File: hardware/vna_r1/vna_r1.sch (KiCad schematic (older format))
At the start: 0 parts

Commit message: layout on vna r1 control board
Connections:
- net labels added: 3V3_DEMOD_EXT_EN
- net labels removed: 3V3_RF_SENSE, AMP_5V, PANEL_PORT1_LED, PANEL_PORT2_LED, PORT1_BIAS, PORT2_BIAS, SPI_CLK, SPI_SDI
- wire segments 193 -> 153
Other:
- note added: "microwave vector network analyzer control board"
- note removed: "microwave vector network analyzer"

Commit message: added adrf5020 breakout
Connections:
- net labels removed: PANEL_POWER_LED
- wire segments 153 -> 151
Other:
- note added: "use Molex Picoblade?\n0151341400\n"
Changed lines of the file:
@@
 F0 "power" 60
 F1 "power.sch" 60
-F4 "3V3_DEMOD_SENSE" I R 3550 2400 60
-F6 "3V3_DEMOD_EN" I L 1650 1800 60
-F9 "3V3_PLL_EN" I L 1650 1900 60
-F10 "3V3_PLL_SENSE" I R 3550 2600 60
+F2 "3V3_DEMOD_SENSE" I R 3550 2400 60
+F3 "3V3_DEMOD_EN" I L 1650 1800 60
+F4 "3V3_PLL_EN" I L 1650 1900 60
+F5 "3V3_PLL_SENSE" I R 3550 2600 60
 $EndSheet
 $Sheet
@@
 F4 "DEMOD_3" O L 12500 7600 60
 F5 "DEMOD_4" O L 12500 9700 60
-F6 "POWER_LED" I R 13800 9400 60
 $EndSheet
 Text Label 14150 6600 0    60   ~ 0
@@
 Text Label 14600 5700 0    60   ~ 0
 RF_SPI_SDI
-Text Label 14000 9400 0    60   ~ 0
-PANEL_POWER_LED
 Text Label 14300 4300 0    60   ~ 0
 PORT_SEL
@@
 Text Label 1500 7350 2    60   ~ 0
 AD_CLKOUT
-Text Label 1500 8900 2    60   ~ 0
-PANEL_POWER_LED
 Text Label 4800 8850 2    60   ~ 0
 EXT_PLL_REF
@@
 F30 "AD_PD" O L 1650 6900 60
 F31 "AD_PC" O L 1650 7000 60
-F32 "PANEL_POWER_LED" O L 1650 8900 60
 F33 "EXT_IO_0" B R 3550 10300 60
 F34 "EXT_IO_1" B R 3550 10400 60
@@
 	9250 10700 9450 10700
 Wire Wire Line
-	13800 9400 14000 9400
-Wire Wire Line
 	4800 8600 5000 8600
 Wire Wire Line
@@
 Wire Wire Line
 	1500 8500 1650 8500
-Wire Wire Line
-	1500 8900 1650 8900
 Wire Wire Line
 	1500 6450 1650 6450
@@
 Text Label 14300 8700 0    60   ~ 0
 3V3_DEMOD_EXT_EN
+Text Notes 14600 7050 0    60   ~ 0
+use Molex Picoblade?\n0151341400\n
 $EndSCHEMATC

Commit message: more work on vna r1..
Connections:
- net labels added: 3V3_LO_EN, LO_-5V_EN, LO_AMP_EN, LO_DAC_CS, LO_PORT_SEL, RF_-5V_EN, RF_PORT_SEL
- net labels removed: -5V_EN, PORT_SEL
- wire segments 151 -> 153
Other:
- note removed: "use Molex Picoblade?\n0151341400\n"
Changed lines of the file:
@@
 F5 "3V3_PLL_SENSE" I R 3550 2600 60
 $EndSheet
-$Sheet
-S 12500 950  1300 8900
-U 59CEBE41
-F0 "front_panel" 60
-F1 "front_panel.sch" 60
-F2 "DEMOD_1" O L 12500 3450 60
-F3 "DEMOD_2" O L 12500 5550 60
-F4 "DEMOD_3" O L 12500 7600 60
-F5 "DEMOD_4" O L 12500 9700 60
-$EndSheet
-Text Label 14150 6600 0    60   ~ 0
+Text Label 14400 8350 0    60   ~ 0
 SYNTH_REF_AP
-Text Label 14150 6700 0    60   ~ 0
+Text Label 14400 8450 0    60   ~ 0
 SYNTH_REF_AN
-Text Label 14550 7950 0    60   ~ 0
+Text Label 14400 8700 0    60   ~ 0
 SYNTH_REF_BP
-Text Label 14550 8050 0    60   ~ 0
+Text Label 14400 8800 0    60   ~ 0
 SYNTH_REF_BN
 Text Label 9250 3400 2    60   ~ 0
@@
 Text Label 9250 9500 2    60   ~ 0
 IF_REF_D
-Text Label 14300 8500 0    60   ~ 0
+Text Label 14350 9050 0    60   ~ 0
 MIX_X2
-Text Label 14300 8600 0    60   ~ 0
+Text Label 14350 9150 0    60   ~ 0
 MIX_EN
 Text Label 9250 5850 2    60   ~ 0
@@
 NoConn ~ 9250 10500
 NoConn ~ 9250 10700
-Text Label 14550 7750 0    60   ~ 0
+Text Label 14350 7600 0    60   ~ 0
 LO_SYNTH_LOCK
-Text Label 14550 7350 0    60   ~ 0
+Text Label 14350 7300 0    60   ~ 0
 LO_SYNTH_CE
-Text Label 14550 7450 0    60   ~ 0
+Text Label 14350 7400 0    60   ~ 0
 LO_SYNTH_CS
-Text Label 14550 7550 0    60   ~ 0
+Text Label 14350 7800 0    60   ~ 0
 LO_SPI_CLK
-Text Label 14550 7650 0    60   ~ 0
+Text Label 14350 7500 0    60   ~ 0
 LO_SPI_SDI
-Text Label 14600 5400 0    60   ~ 0
+Text Label 14350 6400 0    60   ~ 0
 RF_SYNTH_LOCK
-Text Label 14600 5200 0    60   ~ 0
+Text Label 14350 6100 0    60   ~ 0
 RF_SYNTH_CE
-Text Label 14600 5300 0    60   ~ 0
+Text Label 14350 6200 0    60   ~ 0
 RF_SYNTH_CS
-Text Label 14600 5600 0    60   ~ 0
+Text Label 14350 6550 0    60   ~ 0
 RF_SPI_CLK
-Text Label 14600 5500 0    60   ~ 0
+Text Label 14350 6500 0    60   ~ 0
 RF_DAC_CS
-Text Label 14600 5700 0    60   ~ 0
+Text Label 14350 6300 0    60   ~ 0
 RF_SPI_SDI
-Text Label 14300 4300 0    60   ~ 0
-PORT_SEL
+Text Label 14350 5600 0    60   ~ 0
+RF_PORT_SEL
 Text Label 1500 3200 2    60   ~ 0
-PORT_SEL
+RF_PORT_SEL
 Text Label 7100 9700 0    60   ~ 0
 ADC_CLK_D
@@
 Text Label 1500 5400 2    60   ~ 0
 SCL
-Text Label 14600 5950 0    60   ~ 0
+Text Label 14350 5900 0    60   ~ 0
 RF_FILT_SW_1
-Text Label 14650 6250 0    60   ~ 0
+Text Label 14350 7100 0    60   ~ 0
 RF_FILT_SW_2
 Text Label 3750 2400 0    60   ~ 0
@@
 Text Label 3750 2600 0    60   ~ 0
 3V3_PLL_SENSE
-Text Label 14300 4400 0    60   ~ 0
--5V_EN
-Text Label 14300 4500 0    60   ~ 0
+Text Label 14350 5700 0    60   ~ 0
+RF_-5V_EN
+Text Label 14350 5800 0    60   ~ 0
 RF_AMP_EN
-Text Label 14600 5000 0    60   ~ 0
+Text Label 14350 6000 0    60   ~ 0
 3V3_RF_EN
 Text Label 1450 1800 2    60   ~ 0
@@
 RF_FILT_SW_2
 Text Label 1500 5550 2    60   ~ 0
--5V_EN
+RF_-5V_EN
 Text Label 1500 5650 2    60   ~ 0
 RF_AMP_EN
@@
 F30 "AD_PD" O L 1650 6900 60
 F31 "AD_PC" O L 1650 7000 60
-F33 "EXT_IO_0" B R 3550 10300 60
-F34 "EXT_IO_1" B R 3550 10400 60
-F35 "EXT_IO_2" B R 3550 10500 60
-F36 "EXT_IO_3" B R 3550 10600 60
-F37 "EXT_SPI_CS1" O R 3550 9350 60
-F38 "EXT_SPI_CS0" O R 3550 9250 60
-F39 "EXT_SPI_CLK" O R 3550 9600 60
-F40 "EXT_SPI_MISO" I R 3550 9500 60
-F41 "EXT_SPI_MOSI" O R 3550 9700 60
-F42 "EXT_AIN0" I R 3550 10750 60
-F43 "EXT_AIN1" I R 3550 10850 60
-F44 "RF_DAC_CS" O L 1650 4500 60
-F45 "LO_SYNTH_LOCK" O L 1650 4850 60
-F46 "LO_SYNTH_CE" O L 1650 4650 60
-F47 "LO_SYNTH_CS" O L 1650 4750 60
-F48 "EXT_UART_MTX" O R 3550 9950 60
-F49 "EXT_UART_MRX" I R 3550 9850 60
-F50 "LO_SPI_CLK" O L 1650 5000 60
-F51 "LO_SPI_SDI" O L 1650 5100 60
-F52 "RF_SPI_CLK" O L 1650 3600 60
-F53 "RF_SPI_SDI" O L 1650 3700 60
-F54 "EXT_TRIG" I R 3550 10100 60
-F55 "3V3_EXT_DEMOD_EN" O L 1650 6050 61
+F32 "EXT_IO_0" B R 3550 10300 60
+F33 "EXT_IO_1" B R 3550 10400 60
+F34 "EXT_IO_2" B R 3550 10500 60
+F35 "EXT_IO_3" B R 3550 10600 60
+F36 "EXT_SPI_CS1" O R 3550 9350 60
+F37 "EXT_SPI_CS0" O R 3550 9250 60
+F38 "EXT_SPI_CLK" O R 3550 9600 60
+F39 "EXT_SPI_MISO" I R 3550 9500 60
+F40 "EXT_SPI_MOSI" O R 3550 9700 60
+F41 "EXT_AIN0" I R 3550 10750 60
+F42 "EXT_AIN1" I R 3550 10850 60
+F43 "RF_DAC_CS" O L 1650 4500 60
+F44 "LO_SYNTH_LOCK" O L 1650 4850 60
+F45 "LO_SYNTH_CE" O L 1650 4650 60
+F46 "LO_SYNTH_CS" O L 1650 4750 60
+F47 "EXT_UART_MTX" O R 3550 9950 60
+F48 "EXT_UART_MRX" I R 3550 9850 60
+F49 "LO_SPI_CLK" O L 1650 5000 60
+F50 "LO_SPI_SDI" O L 1650 5100 60
+F51 "RF_SPI_CLK" O L 1650 3600 60
+F52 "RF_SPI_SDI" O L 1650 3700 60
+F53 "EXT_TRIG" I R 3550 10100 60
+F54 "3V3_EXT_DEMOD_EN" O L 1650 6050 61
 $EndSheet
 Text Label 14800 1950 2    60   ~ 0
@@
 	11150 3450 12500 3450
 Wire Wire Line
-	14150 6600 13950 6600
-Wire Wire Line
-	14150 6700 13950 6700
-Wire Wire Line
-	14550 7950 14350 7950
-Wire Wire Line
-	14550 8050 14350 8050
-Wire Wire Line
-	14550 7650 14350 7650
-Wire Wire Line
-	14550 7750 14350 7750
-Wire Wire Line
-	14550 7450 14350 7450
-Wire Wire Line
-	14550 7550 14350 7550
-Wire Wire Line
-	14550 7350 14350 7350
-Wire Wire Line
-	14600 5400 14400 5400
-Wire Wire Line
-	14600 5300 14400 5300
-Wire Wire Line
-	14600 5200 14400 5200
-Wire Wire Line
-	14600 5950 14400 5950
-Wire Wire Line
-	14650 6250 14450 6250
-Wire Wire Line
-	14600 5600 14400 5600
-Wire Wire Line
-	14600 5700 14400 5700
-Wire Wire Line
-	14600 5500 14400 5500
+	14400 8350 14200 8350
+Wire Wire Line
+	14400 8450 14200 8450
+Wire Wire Line
+	14400 8700 14200 8700
+Wire Wire Line
+	14400 8800 14200 8800
+Wire Wire Line
+	14350 7500 14150 7500
+Wire Wire Line
+	14350 7600 14150 7600
+Wire Wire Line
+	14350 7400 14150 7400
+Wire Wire Line
+	14350 7800 14150 7800
+Wire Wire Line
+	14350 7300 14150 7300
+Wire Wire Line
+	14350 6400 14150 6400
+Wire Wire Line
+	14350 6200 14150 6200
+Wire Wire Line
+	14350 6100 14150 6100
+Wire Wire Line
+	14350 5900 14150 5900
+Wire Wire Line
+	14350 7100 14150 7100
+Wire Wire Line
+	14350 6550 14150 6550
+Wire Wire Line
+	14350 6300 14150 6300
+Wire Wire Line
+	14350 6500 14150 6500
 Wire Wire Line
 	9250 3250 9450 3250
@@
 	9250 9650 9450 9650
 Wire Wire Line
-	14300 8500 14100 8500
+	14350 9050 14150 9050
 Wire Wire Line
 	9250 5850 9450 5850
@@
 Wire Wire Line
 	1500 6050 1650 6050
-Text Label 14300 8700 0    60   ~ 0
+Text Label 14350 9250 0    60   ~ 0
 3V3_DEMOD_EXT_EN
-Text Notes 14600 7050 0    60   ~ 0
-use Molex Picoblade?\n0151341400\n
+Text Label 14350 7200 0    60   ~ 0
+3V3_LO_EN
+Text Label 4400 5200 2    60   ~ 0
+3V3_LO_EN
+Wire Wire Line
+	14350 7200 14150 7200
+Text Label 14350 7700 0    60   ~ 0
+LO_DAC_CS
+Wire Wire Line
+	14350 7700 14150 7700
+Text Label 4300 5400 2    60   ~ 0
+LO_DAC_CS
+Text Label 14350 6800 0    60   ~ 0
+LO_PORT_SEL
+Text Label 14350 6900 0    60   ~ 0
+LO_-5V_EN
+Text Label 14350 7000 0    60   ~ 0
+LO_AMP_EN
+Text Label 3900 5750 0    60   ~ 0
+LO_PORT_SEL
+Text Label 3900 5850 0    60   ~ 0
+LO_-5V_EN
+Text Label 3900 5950 0    60   ~ 0
+LO_AMP_EN
+$Sheet
+S 12500 950  1650 8900
+U 59CEBE41
+F0 "front_panel" 60
+F1 "front_panel.sch" 60
+F2 "DEMOD_1" O L 12500 3450 60
+F3 "DEMOD_2" O L 12500 5550 60
+F4 "DEMOD_3" O L 12500 7600 60
+F5 "DEMOD_4" O L 12500 9700 60
+F6 "RF_PORT_SEL" I R 14150 5550 60
+F7 "RF_-5V_EN" I R 14150 5650 60
+F8 "RF_AMP_EN" I R 14150 5750 60
+F9 "RF_FILT_SW_1" I R 14150 5850 60
+F10 "RF_3V3_EN" I R 14150 5950 60
+F11 "RF_SYNTH_CE" I R 14150 6050 60
+F12 "RF_SYNTH_CS" I R 14150 6150 60
+F13 "RF_SYNTH_SDI" I R 14150 6250 60
+F14 "RF_SYNTH_LOCK" I R 14150 6350 60
+F15 "RF_DAC_CS" I R 14150 6450 60
+F16 "LO_PORT_SEL" I R 14150 6800 60
+F17 "LO_-5V_EN" I R 14150 6900 60
+F18 "LO_AMP_EN" I R 14150 7000 60
+F19 "LO_FILT_SW_1" I R 14150 7100 60
+F20 "LO_3V3_EN" I R 14150 7200 60
+F21 "LO_SYNTH_CE" I R 14150 7300 60
+F22 "LO_SYNTH_CS" I R 14150 7400 60
+F23 "LO_SYNTH_SDI" I R 14150 7500 60
+F24 "LO_SYNTH_LOCK" I R 14150 7600 60
+F25 "LO_DAC_CS" I R 14150 7700 60
+F26 "LO_SYNTH_REF_P" I R 14150 8350 60
+F27 "LO_SYNTH_REF_N" I R 14150 8450 60
+F28 "RF_SYNTH_REF_P" I R 14150 8700 60
+F29 "RF_SYNTH_REF_N" I R 14150 8800 60
+F30 "MIX_X2" I R 14150 9050 60
+F31 "MIX_EN" I R 14150 9150 60
+F32 "MIX_3V3_EN" I R 14150 9250 60
+F33 "LO_SYNTH_CLK" I R 14150 7800 60
+F34 "RF_SYNTH_CLK" I R 14150 6550 60
+$EndSheet
 $EndSCHEMATC

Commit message: work on vna r1 synth board
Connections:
- net labels added: LO_3V3_EN, RF_3V3_EN
- net labels removed: 3V3_LO_EN, 3V3_RF_EN
- wire segments 153 -> 167

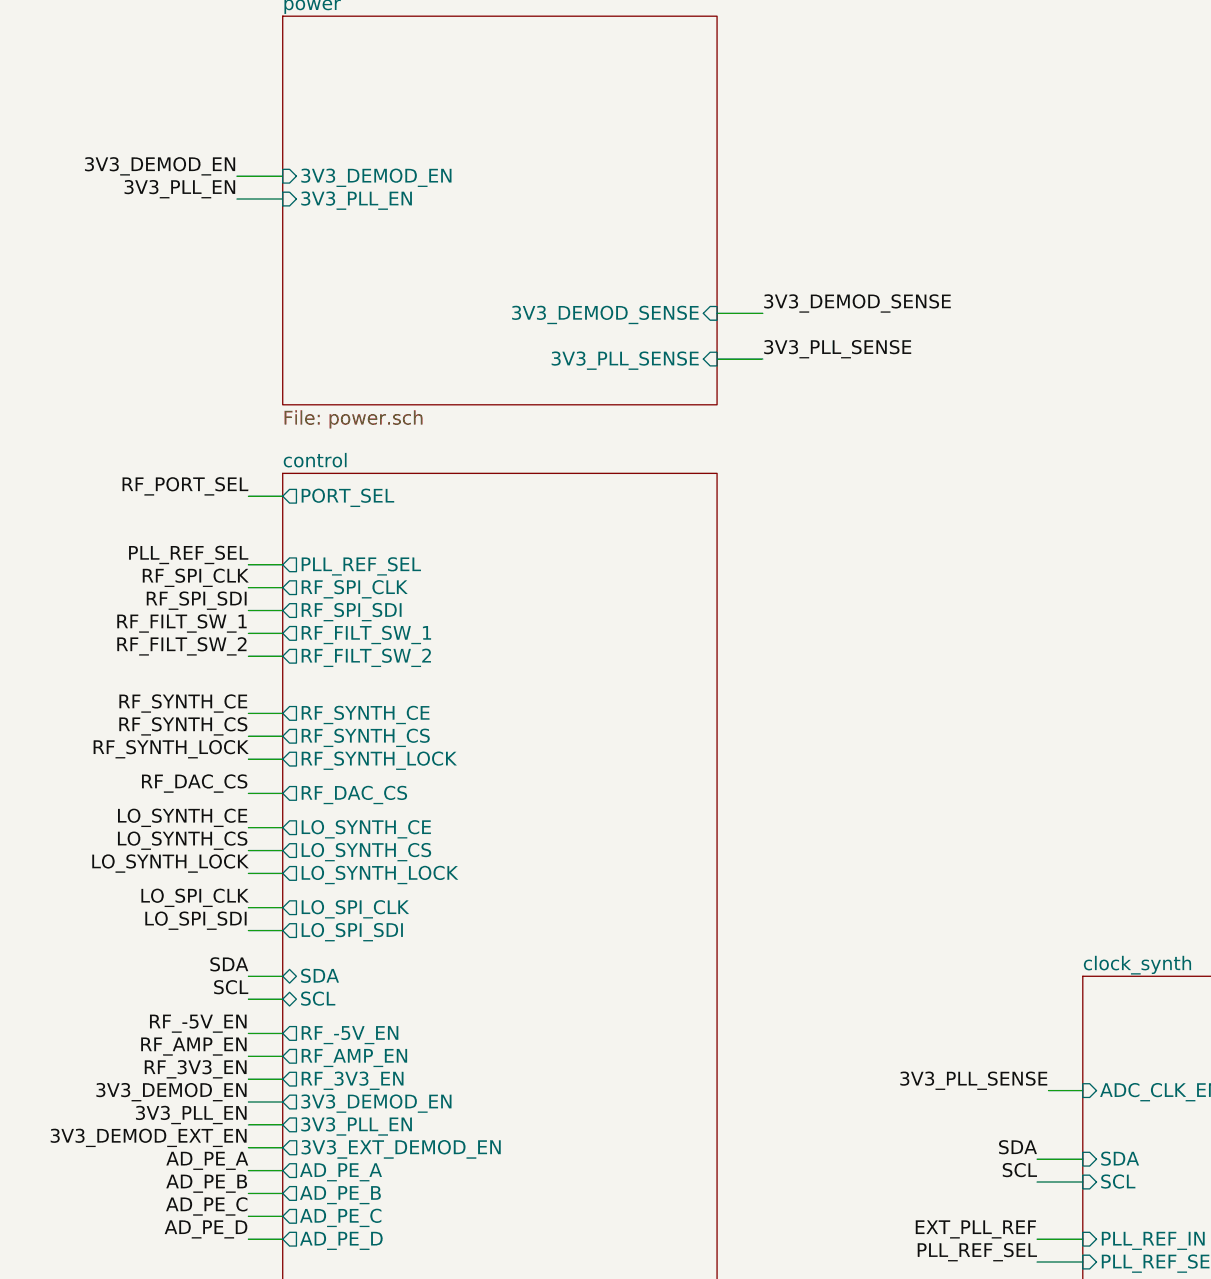
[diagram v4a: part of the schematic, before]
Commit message: added measured data on r2 directional coupler
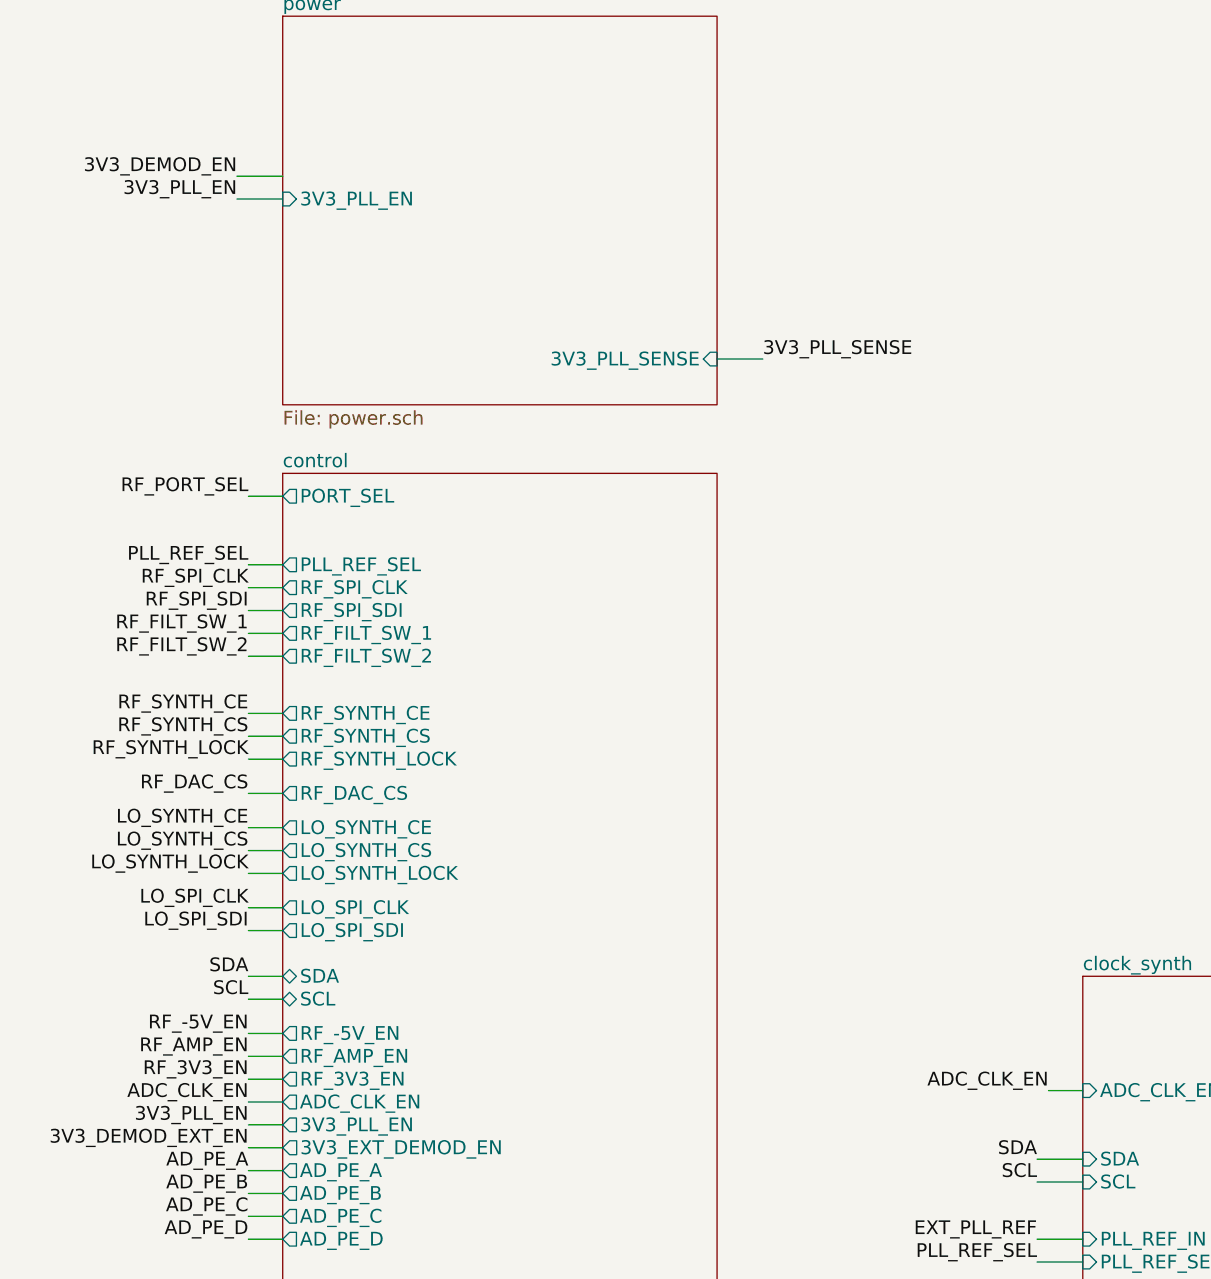
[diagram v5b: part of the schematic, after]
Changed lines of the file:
@@
 F0 "power" 60
 F1 "power.sch" 60
-F2 "3V3_DEMOD_SENSE" I R 3550 2400 60
-F3 "3V3_DEMOD_EN" I L 1650 1800 60
 F4 "3V3_PLL_EN" I L 1650 1900 60
 F5 "3V3_PLL_SENSE" I R 3550 2600 60
@@
 Text Label 14350 7100 0    60   ~ 0
 RF_FILT_SW_2
-Text Label 3750 2400 0    60   ~ 0
-3V3_DEMOD_SENSE
 Text Label 3750 2600 0    60   ~ 0
 3V3_PLL_SENSE
@@
 Text Label 1500 5750 2    60   ~ 0
 RF_3V3_EN
-Text Label 1500 5850 2    60   ~ 0
-3V3_DEMOD_EN
 Text Label 1500 5950 2    60   ~ 0
 3V3_PLL_EN
-Text Label 5000 5800 2    60   ~ 0
-3V3_PLL_SENSE
 Text Label 1500 6450 2    60   ~ 0
 AD_PE_D
@@
 F1 "control.sch" 60
 F2 "PLL_REF_SEL" O L 1650 3500 60
-F3 "3V3_DEMOD_EN" O L 1650 5850 60
-F4 "3V3_PLL_EN" O L 1650 5950 60
-F5 "RF_AMP_EN" O L 1650 5650 60
-F6 "MIX_X2" O L 1650 8400 60
-F7 "MIX_EN" O L 1650 8500 60
-F8 "AD_DOUTD" I L 1650 7850 60
-F9 "AD_DOUTC" I L 1650 7750 60
-F10 "AD_DOUTB" I L 1650 7650 60
-F11 "AD_DOUTA" I L 1650 7550 60
-F12 "AD_SYNCB" O L 1650 7150 60
-F13 "AD_FS" I L 1650 7250 60
-F14 "AD_CLKOUT" I L 1650 7350 60
-F15 "PORT_SEL" O L 1650 3200 60
-F16 "RF_FILT_SW_1" O L 1650 3800 60
-F17 "RF_FILT_SW_2" O L 1650 3900 60
-F18 "RF_SYNTH_CE" O L 1650 4150 60
-F19 "RF_SYNTH_CS" O L 1650 4250 60
-F20 "RF_SYNTH_LOCK" O L 1650 4350 60
-F21 "SCL" B L 1650 5400 60
-F22 "SDA" B L 1650 5300 60
-F23 "AD_PE_C" O L 1650 6350 60
-F24 "AD_PE_D" O L 1650 6450 60
-F25 "AD_PE_B" O L 1650 6250 60
-F26 "AD_PE_A" O L 1650 6150 60
-F27 "AD_DOUT_B" I L 1650 6800 60
-F28 "AD_PD" O L 1650 6900 60
-F29 "AD_PC" O L 1650 7000 60
-F30 "EXT_IO_0" B R 3550 10300 60
-F31 "EXT_IO_1" B R 3550 10400 60
-F32 "EXT_IO_2" B R 3550 10500 60
-F33 "EXT_IO_3" B R 3550 10600 60
-F34 "EXT_SPI_CS1" O R 3550 9350 60
-F35 "EXT_SPI_CS0" O R 3550 9250 60
-F36 "EXT_SPI_CLK" O R 3550 9600 60
-F37 "EXT_SPI_MISO" I R 3550 9500 60
-F38 "EXT_SPI_MOSI" O R 3550 9700 60
-F39 "EXT_AIN0" I R 3550 10750 60
-F40 "EXT_AIN1" I R 3550 10850 60
-F41 "RF_DAC_CS" O L 1650 4500 60
-F42 "LO_SYNTH_LOCK" O L 1650 4850 60
-F43 "LO_SYNTH_CE" O L 1650 4650 60
-F44 "LO_SYNTH_CS" O L 1650 4750 60
-F45 "EXT_UART_MTX" O R 3550 9950 60
-F46 "EXT_UART_MRX" I R 3550 9850 60
-F47 "LO_SPI_CLK" O L 1650 5000 60
-F48 "LO_SPI_SDI" O L 1650 5100 60
-F49 "RF_SPI_CLK" O L 1650 3600 60
-F50 "RF_SPI_SDI" O L 1650 3700 60
-F51 "EXT_TRIG" I R 3550 10100 60
-F52 "3V3_EXT_DEMOD_EN" O L 1650 6050 61
-F53 "RF_3V3_EN" O L 1650 5750 60
-F54 "RF_-5V_EN" O L 1650 5550 60
-F55 "LO_AMP_EN" I L 1650 8750 60
-F56 "LO_-5V_EN" I L 1650 8850 60
-F57 "LO_3V3_EN" I L 1650 8950 60
-F58 "LO_PORT_SEL" I L 1650 9050 60
-F59 "LO_DAC_CS" I L 1650 9150 60
+F3 "3V3_PLL_EN" O L 1650 5950 60
+F4 "RF_AMP_EN" O L 1650 5650 60
+F5 "MIX_X2" O L 1650 8400 60
+F6 "MIX_EN" O L 1650 8500 60
+F7 "AD_DOUTD" I L 1650 7850 60
+F8 "AD_DOUTC" I L 1650 7750 60
+F9 "AD_DOUTB" I L 1650 7650 60
+F10 "AD_DOUTA" I L 1650 7550 60
+F11 "AD_SYNCB" O L 1650 7150 60
+F12 "AD_FS" I L 1650 7250 60
+F13 "AD_CLKOUT" I L 1650 7350 60
+F14 "PORT_SEL" O L 1650 3200 60
+F15 "RF_FILT_SW_1" O L 1650 3800 60
+F16 "RF_FILT_SW_2" O L 1650 3900 60
+F17 "RF_SYNTH_CE" O L 1650 4150 60
+F18 "RF_SYNTH_CS" O L 1650 4250 60
+F19 "RF_SYNTH_LOCK" O L 1650 4350 60
+F20 "SCL" B L 1650 5400 60
+F21 "SDA" B L 1650 5300 60
+F22 "AD_PE_C" O L 1650 6350 60
+F23 "AD_PE_D" O L 1650 6450 60
+F24 "AD_PE_B" O L 1650 6250 60
+F25 "AD_PE_A" O L 1650 6150 60
+F26 "AD_DOUT_B" I L 1650 6800 60
+F27 "AD_PD" O L 1650 6900 60
+F28 "AD_PC" O L 1650 7000 60
+F29 "EXT_IO_0" B R 3550 10300 60
+F30 "EXT_IO_1" B R 3550 10400 60
+F31 "EXT_IO_2" B R 3550 10500 60
+F32 "EXT_IO_3" B R 3550 10600 60
+F33 "EXT_SPI_CS1" O R 3550 9350 60
+F34 "EXT_SPI_CS0" O R 3550 9250 60
+F35 "EXT_SPI_CLK" O R 3550 9600 60
+F36 "EXT_SPI_MISO" I R 3550 9500 60
+F37 "EXT_SPI_MOSI" O R 3550 9700 60
+F38 "EXT_AIN0" I R 3550 10750 60
+F39 "EXT_AIN1" I R 3550 10850 60
+F40 "RF_DAC_CS" O L 1650 4500 60
+F41 "LO_SYNTH_LOCK" O L 1650 4850 60
+F42 "LO_SYNTH_CE" O L 1650 4650 60
+F43 "LO_SYNTH_CS" O L 1650 4750 60
+F44 "EXT_UART_MTX" O R 3550 9950 60
+F45 "EXT_UART_MRX" I R 3550 9850 60
+F46 "LO_SPI_CLK" O L 1650 5000 60
+F47 "LO_SPI_SDI" O L 1650 5100 60
+F48 "RF_SPI_CLK" O L 1650 3600 60
+F49 "RF_SPI_SDI" O L 1650 3700 60
+F50 "EXT_TRIG" I R 3550 10100 60
+F51 "3V3_EXT_DEMOD_EN" O L 1650 6050 61
+F52 "RF_3V3_EN" O L 1650 5750 60
+F53 "RF_-5V_EN" O L 1650 5550 60
+F54 "LO_AMP_EN" I L 1650 8750 60
+F55 "LO_-5V_EN" I L 1650 8850 60
+F56 "LO_3V3_EN" I L 1650 8950 60
+F57 "LO_PORT_SEL" I L 1650 9050 60
+F58 "LO_DAC_CS" I L 1650 9150 60
+F59 "ADC_CLK_EN" O L 1650 5850 60
 $EndSheet
 Text Label 14900 1900 2    60   ~ 0
@@
 	1450 1900 1650 1900
 Wire Wire Line
-	3550 2400 3750 2400
-Wire Wire Line
 	3550 2600 3750 2600
 Wire Wire Line
@@
 Wire Wire Line
 	1500 5950 1650 5950
-Wire Wire Line
-	1500 5850 1650 5850
 Wire Wire Line
 	1500 5750 1650 5750
@@
 Wire Wire Line
 	1500 9150 1650 9150
+Text Label 5000 5800 2    60   ~ 0
+ADC_CLK_EN
+Text Label 1500 5850 2    60   ~ 0
+ADC_CLK_EN
+Wire Wire Line
+	1650 5850 1500 5850
 $EndSCHEMATC
